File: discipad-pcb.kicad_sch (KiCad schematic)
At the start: 56 parts

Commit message: changed button footprint
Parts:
- ?: footprint (none) -> Button_Switch_SMD:SW_SPST_SKQG_WithStem
- ?: footprint Button_Switch_THT:SW_PUSH_6mm -> Button_Switch_SMD:SW_SPST_SKQG_WithStem
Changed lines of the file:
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@@
     (property "Reference" "" (id 0) (at 71.755 114.808 0))
     (property "Value" "BOOT" (id 1) (at 71.755 117.1194 0))
-    (property "Footprint" "" (id 2) (at 71.755 121.285 0)
-      (effects (font (size 1.524 1.524)))
+    (property "Footprint" "Button_Switch_SMD:SW_SPST_SKQG_WithStem" (id 2) (at 71.755 121.285 0)
+      (effects (font (size 1.524 1.524)) hide)
     )
     (property "Datasheet" "" (id 3) (at 71.755 121.285 0)
@@
     (property "Reference" "" (id 0) (at 71.755 133.858 0))
     (property "Value" "RESET" (id 1) (at 71.755 136.1694 0))
-    (property "Footprint" "Button_Switch_THT:SW_PUSH_6mm" (id 2) (at 71.755 140.335 0)
+    (property "Footprint" "Button_Switch_SMD:SW_SPST_SKQG_WithStem" (id 2) (at 71.755 140.335 0)
       (effects (font (size 1.524 1.524)) hide)
     )
@@
     )
     (path "/00000000-0000-0000-0000-00005d2c0447"
-      (reference "BOOT1") (unit 1) (value "BOOT") (footprint "")
+      (reference "BOOT1") (unit 1) (value "BOOT") (footprint "Button_Switch_SMD:SW_SPST_SKQG_WithStem")
     )
     (path "/00000000-0000-0000-0000-00005d2f4a78"
@@
     )
     (path "/00000000-0000-0000-0000-00005d2fcd08"
-      (reference "RESET1") (unit 1) (value "RESET") (footprint "Button_Switch_THT:SW_PUSH_6mm")
+      (reference "RESET1") (unit 1) (value "RESET") (footprint "Button_Switch_SMD:SW_SPST_SKQG_WithStem")
     )
     (path "/00000000-0000-0000-0000-00005bdaa9a5"

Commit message: added footprint to status led
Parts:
- ?: footprint (none) -> LED_SMD:LED_0805_2012Metric_Pad1.15x1.40mm_HandSolder
- ?: footprint (none) -> Resistor_THT:R_Axial_DIN0204_L3.6mm_D1.6mm_P5.08mm_Horizontal
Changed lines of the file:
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@@
     (property "Reference" "" (id 0) (at 208.4832 117.348 0))
     (property "Value" "POWER" (id 1) (at 208.4832 119.6594 0))
-    (property "Footprint" "" (id 2) (at 208.28 123.825 0)
+    (property "Footprint" "LED_SMD:LED_0805_2012Metric_Pad1.15x1.40mm_HandSolder" (id 2) (at 208.28 123.825 0)
       (effects (font (size 1.27 1.27)) hide)
     )
@@
     (property "Reference" "" (id 0) (at 198.12 118.8466 90))
     (property "Value" "1.5K" (id 1) (at 198.12 121.158 90))
-    (property "Footprint" "" (id 2) (at 198.12 123.825 0)
+    (property "Footprint" "Resistor_THT:R_Axial_DIN0204_L3.6mm_D1.6mm_P5.08mm_Horizontal" (id 2) (at 198.12 123.825 0)
       (effects (font (size 1.27 1.27)) hide)
     )
@@
     )
     (path "/00000000-0000-0000-0000-00005d2c3a43"
-      (reference "LED1") (unit 1) (value "POWER") (footprint "")
+      (reference "LED1") (unit 1) (value "POWER") (footprint "LED_SMD:LED_0805_2012Metric_Pad1.15x1.40mm_HandSolder")
     )
     (path "/00000000-0000-0000-0000-00005d2daa5c"
@@
     )
     (path "/00000000-0000-0000-0000-00005d2c3c60"
-      (reference "R7") (unit 1) (value "1.5K") (footprint "")
+      (reference "R7") (unit 1) (value "1.5K") (footprint "Resistor_THT:R_Axial_DIN0204_L3.6mm_D1.6mm_P5.08mm_Horizontal")
     )
     (path "/00000000-0000-0000-0000-00005d2fcd08"

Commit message: added avr-isp header
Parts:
- ?: footprint (none) -> Connector_PinHeader_2.54mm:PinHeader_2x03_P2.54mm_Vertical
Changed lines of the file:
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@@
       (effects (font (size 1.27 1.27)) (justify right))
     )
-    (property "Footprint" "" (id 2) (at 245.745 127 90)
+    (property "Footprint" "Connector_PinHeader_2.54mm:PinHeader_2x03_P2.54mm_Vertical" (id 2) (at 245.745 127 90)
       (effects (font (size 1.27 1.27)) hide)
     )
@@
     )
     (path "/00000000-0000-0000-0000-00005d2c325d"
-      (reference "J1") (unit 1) (value "AVR-ISP-6") (footprint "")
+      (reference "J1") (unit 1) (value "AVR-ISP-6") (footprint "Connector_PinHeader_2.54mm:PinHeader_2x03_P2.54mm_Vertical")
     )
     (path "/00000000-0000-0000-0000-00005d2c3a43"

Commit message: added fuse footprint
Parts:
- ?: footprint keyboard_parts:polyfuse_5.1mm -> Fuse:Fuse_Littelfuse_395Series
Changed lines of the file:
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@@
       (effects (font (size 1.27 1.27)) (justify left))
     )
-    (property "Footprint" "keyboard_parts:polyfuse_5.1mm" (id 2) (at 135.89 128.905 0)
+    (property "Footprint" "Fuse:Fuse_Littelfuse_395Series" (id 2) (at 135.89 128.905 0)
       (effects (font (size 1.27 1.27)) (justify left) hide)
     )
@@
     )
     (path "/00000000-0000-0000-0000-00005d2ccadb"
-      (reference "F1") (unit 1) (value "500mA") (footprint "keyboard_parts:polyfuse_5.1mm")
+      (reference "F1") (unit 1) (value "500mA") (footprint "Fuse:Fuse_Littelfuse_395Series")
     )
     (path "/00000000-0000-0000-0000-00005d2c325d"

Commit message: added usb-c footprint
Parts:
- ?: footprint Type-C:USB_C_GCT_USB4085 -> Connector_USB:USB_C_Receptacle_GCT_USB4085
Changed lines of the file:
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@@
       (effects (font (size 1.524 1.524)))
     )
-    (property "Footprint" "Type-C:USB_C_GCT_USB4085" (id 2) (at 120.65 153.035 0)
+    (property "Footprint" "Connector_USB:USB_C_Receptacle_GCT_USB4085" (id 2) (at 120.65 153.035 0)
       (effects (font (size 1.524 1.524)) hide)
     )
@@
     )
     (path "/00000000-0000-0000-0000-00005d2c4195"
-      (reference "USB1") (unit 1) (value "USB_C_GCT_USB4085") (footprint "Type-C:USB_C_GCT_USB4085")
+      (reference "USB1") (unit 1) (value "USB_C_GCT_USB4085") (footprint "Connector_USB:USB_C_Receptacle_GCT_USB4085")
     )
     (path "/00000000-0000-0000-0000-00005d2efb9f"

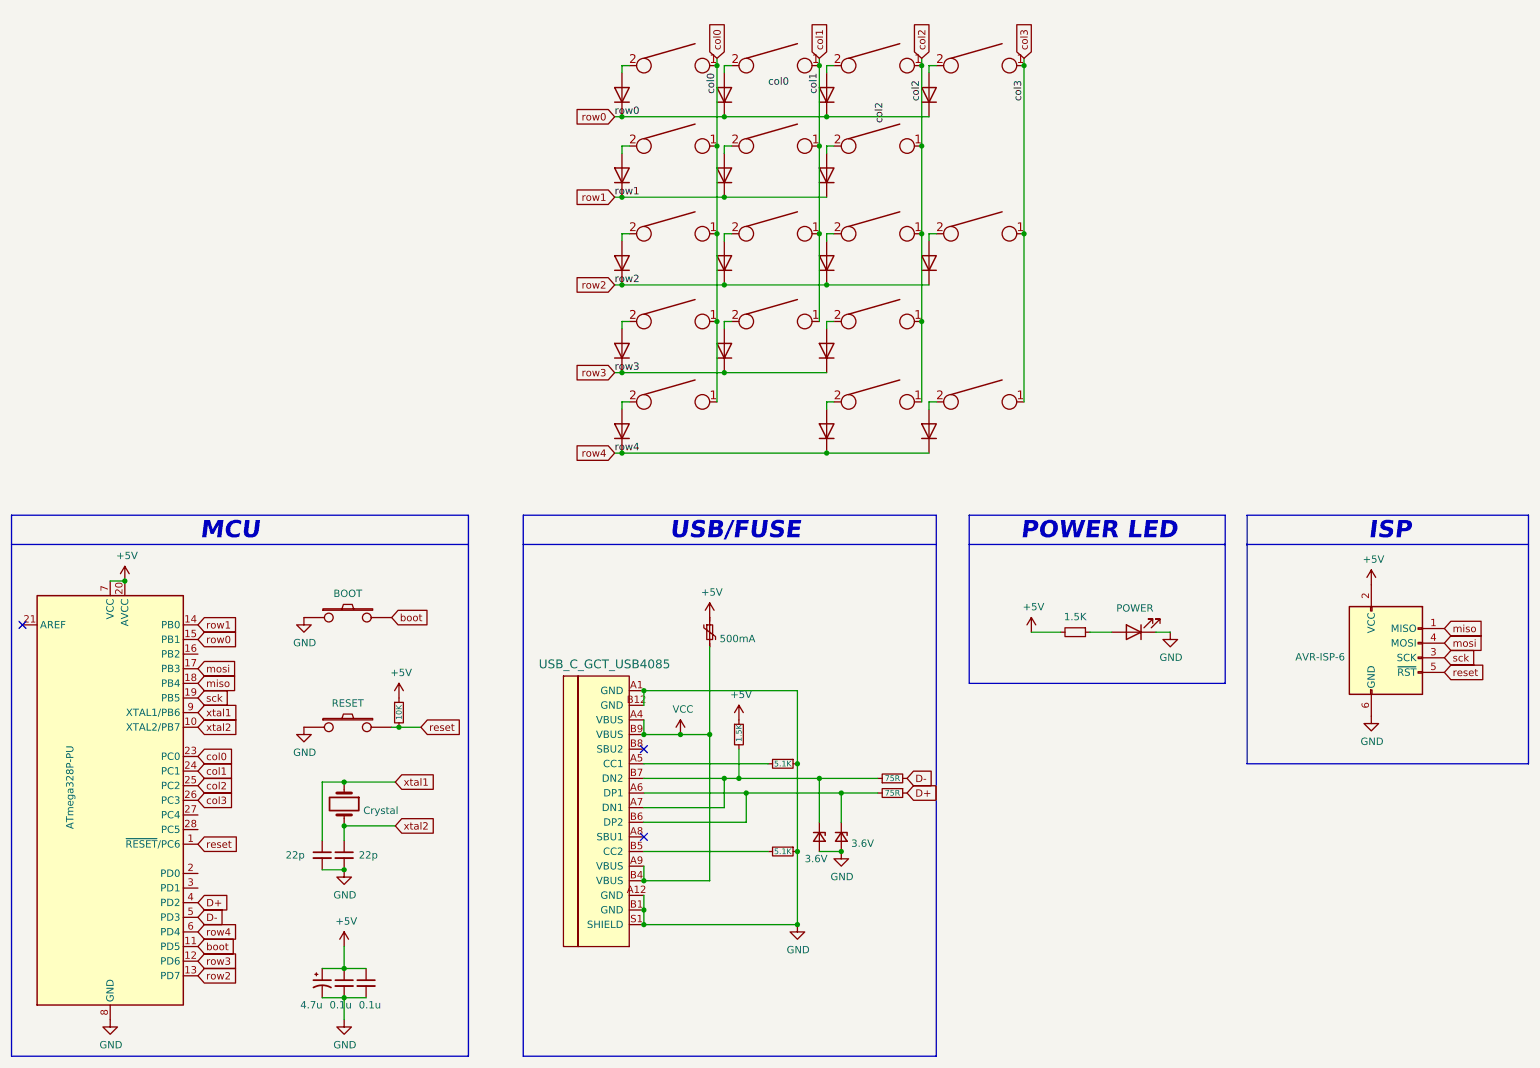
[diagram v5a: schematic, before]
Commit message: changed fuse footprint
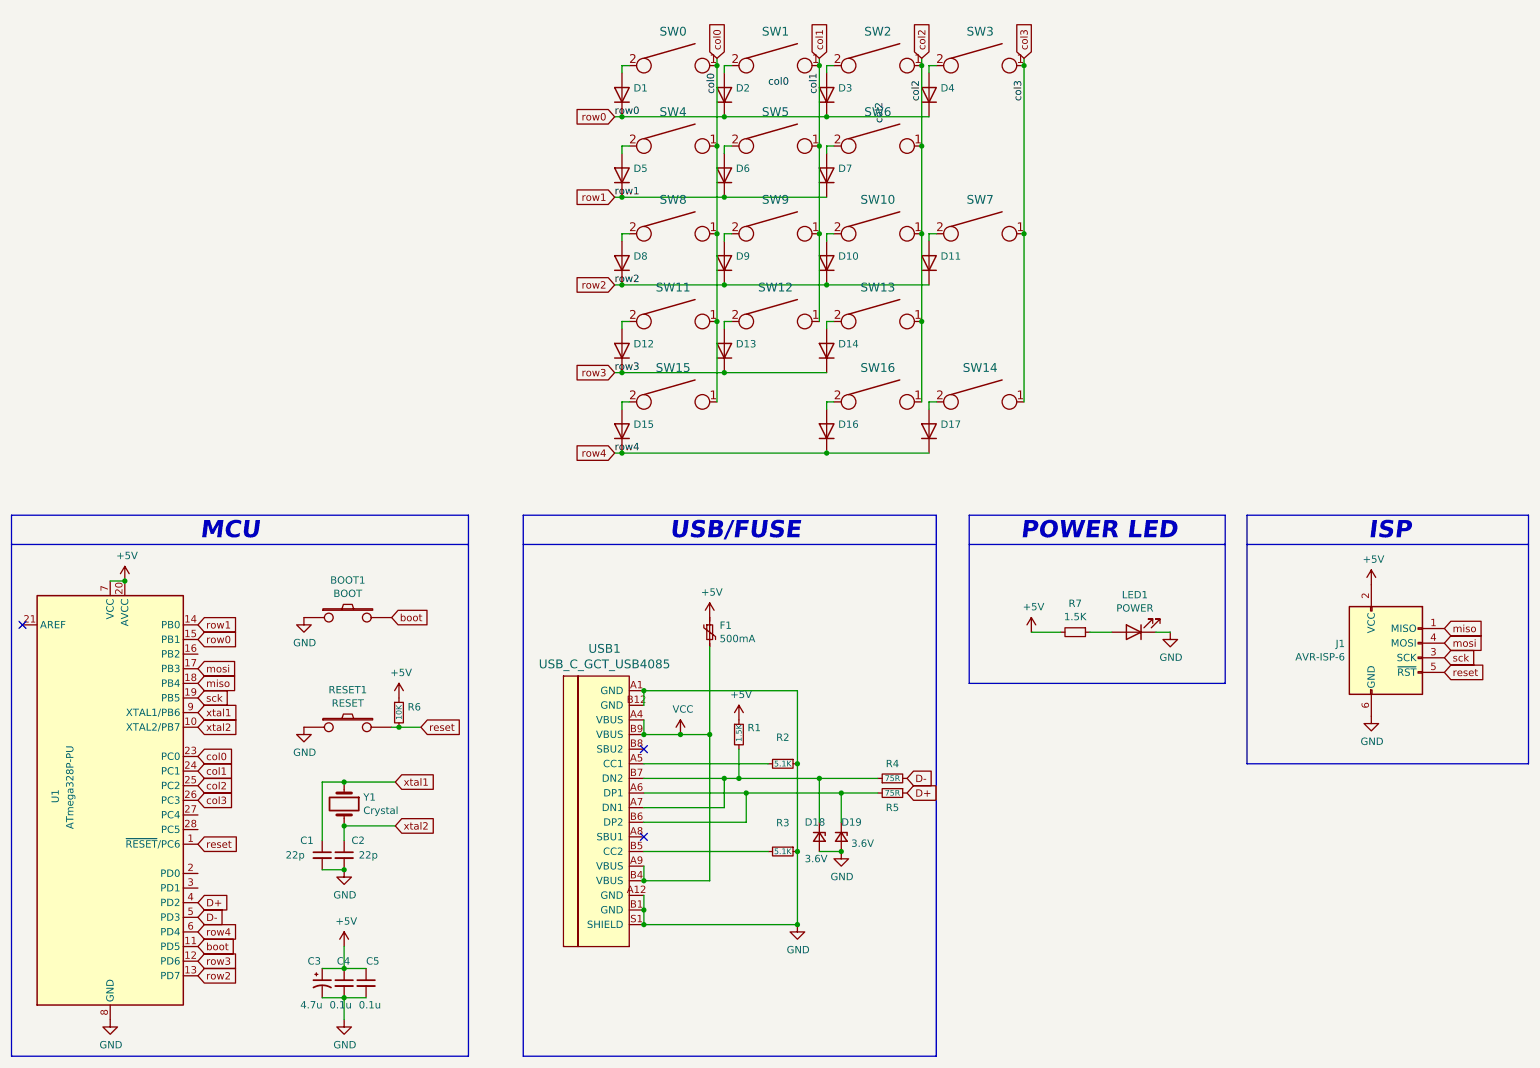
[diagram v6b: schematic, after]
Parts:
- F1: renamed from ?; footprint Fuse:Fuse_Littelfuse_395Series -> led:polyfuse_5.1mm
- gave numbers to parts that had none: 55
